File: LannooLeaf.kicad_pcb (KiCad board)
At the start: 2 copper layers, 348.4 x 351.9 mm, 167 parts, among them J1 Conn_01x01, J12 Conn_02x04_Counter_Clockwise, J2 Conn_01x01, J3 Conn_01x01, J4 Conn_01x01, J5 Conn_02x04_Counter_Clockwise, J6 Conn_02x10_Counter_Clockwise, J7 Conn_02x10_Counter_Clockwise

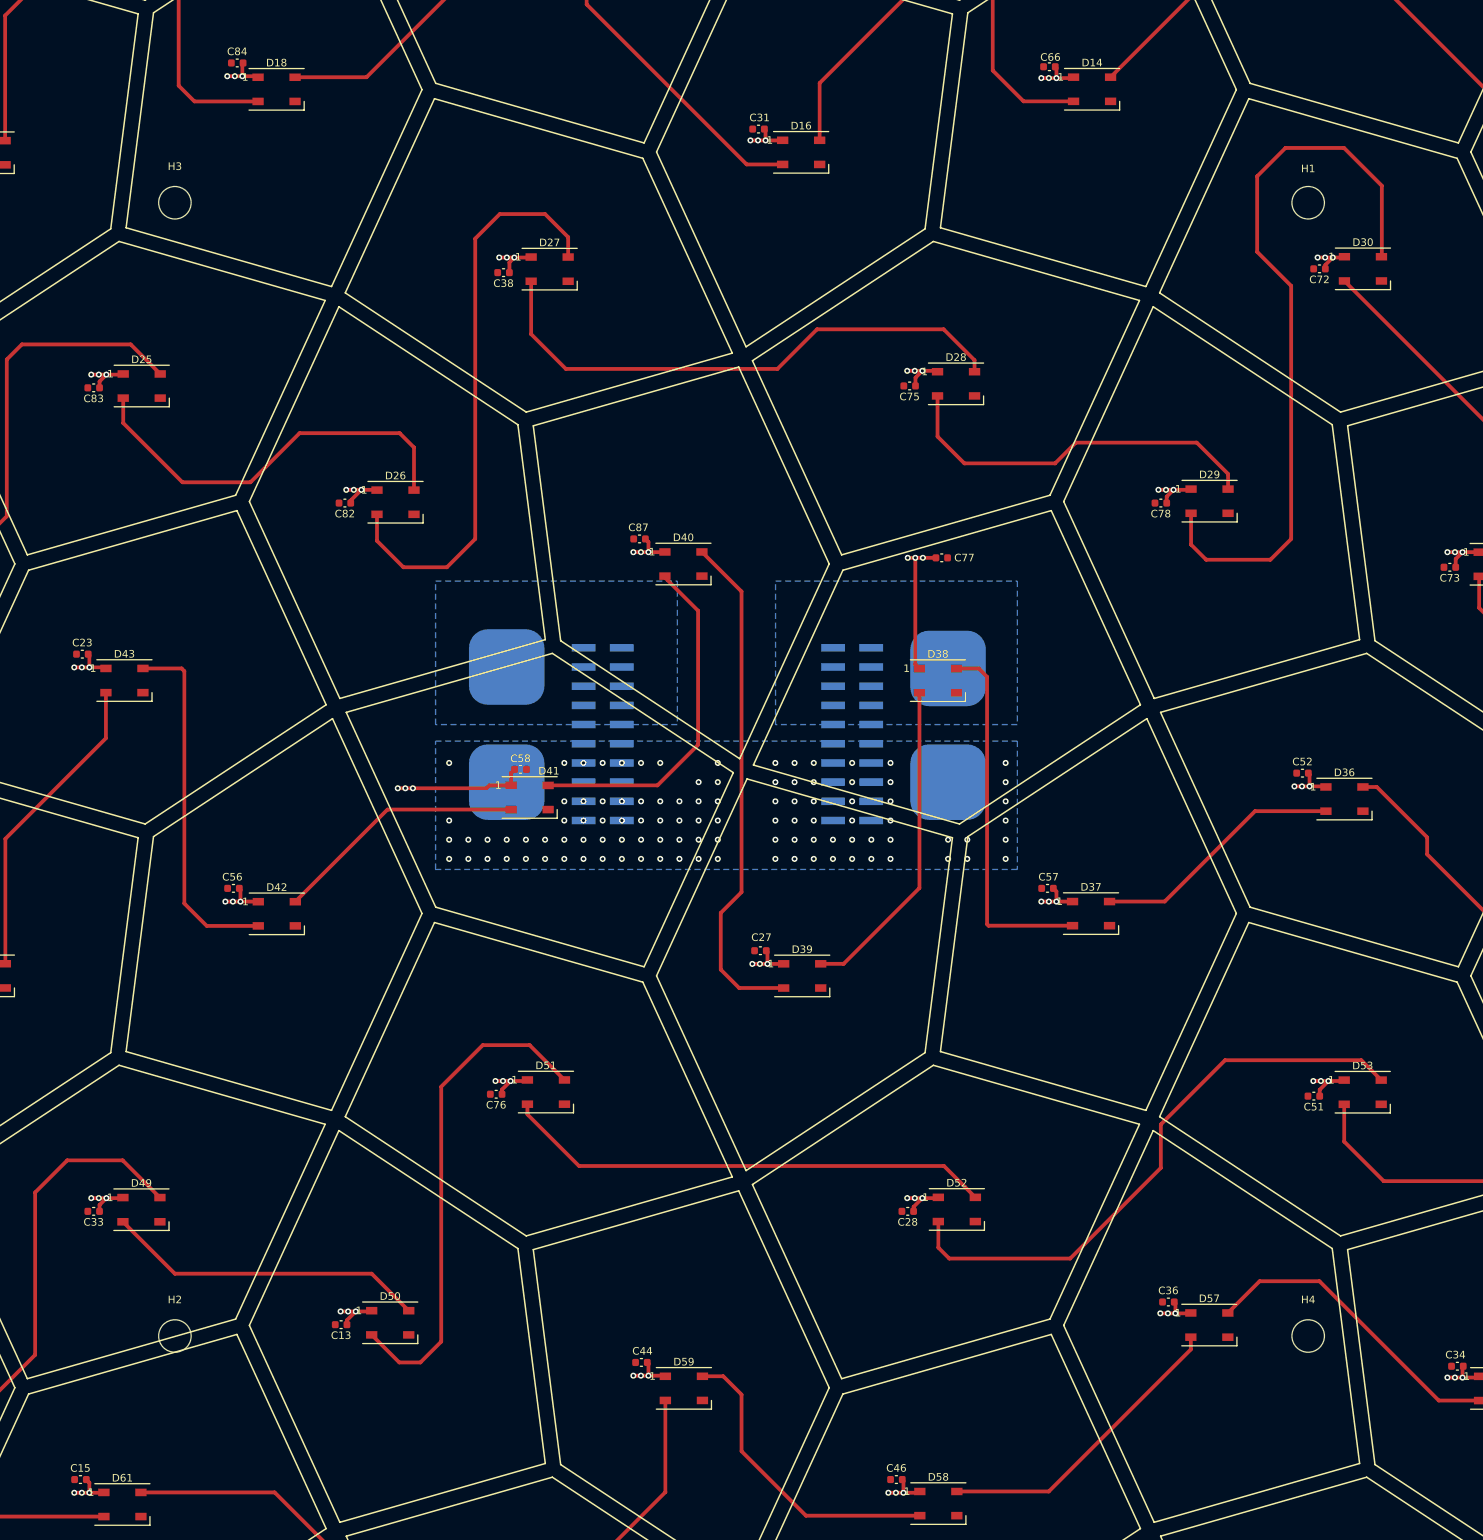
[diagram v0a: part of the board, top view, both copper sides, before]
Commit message: update mountingholes
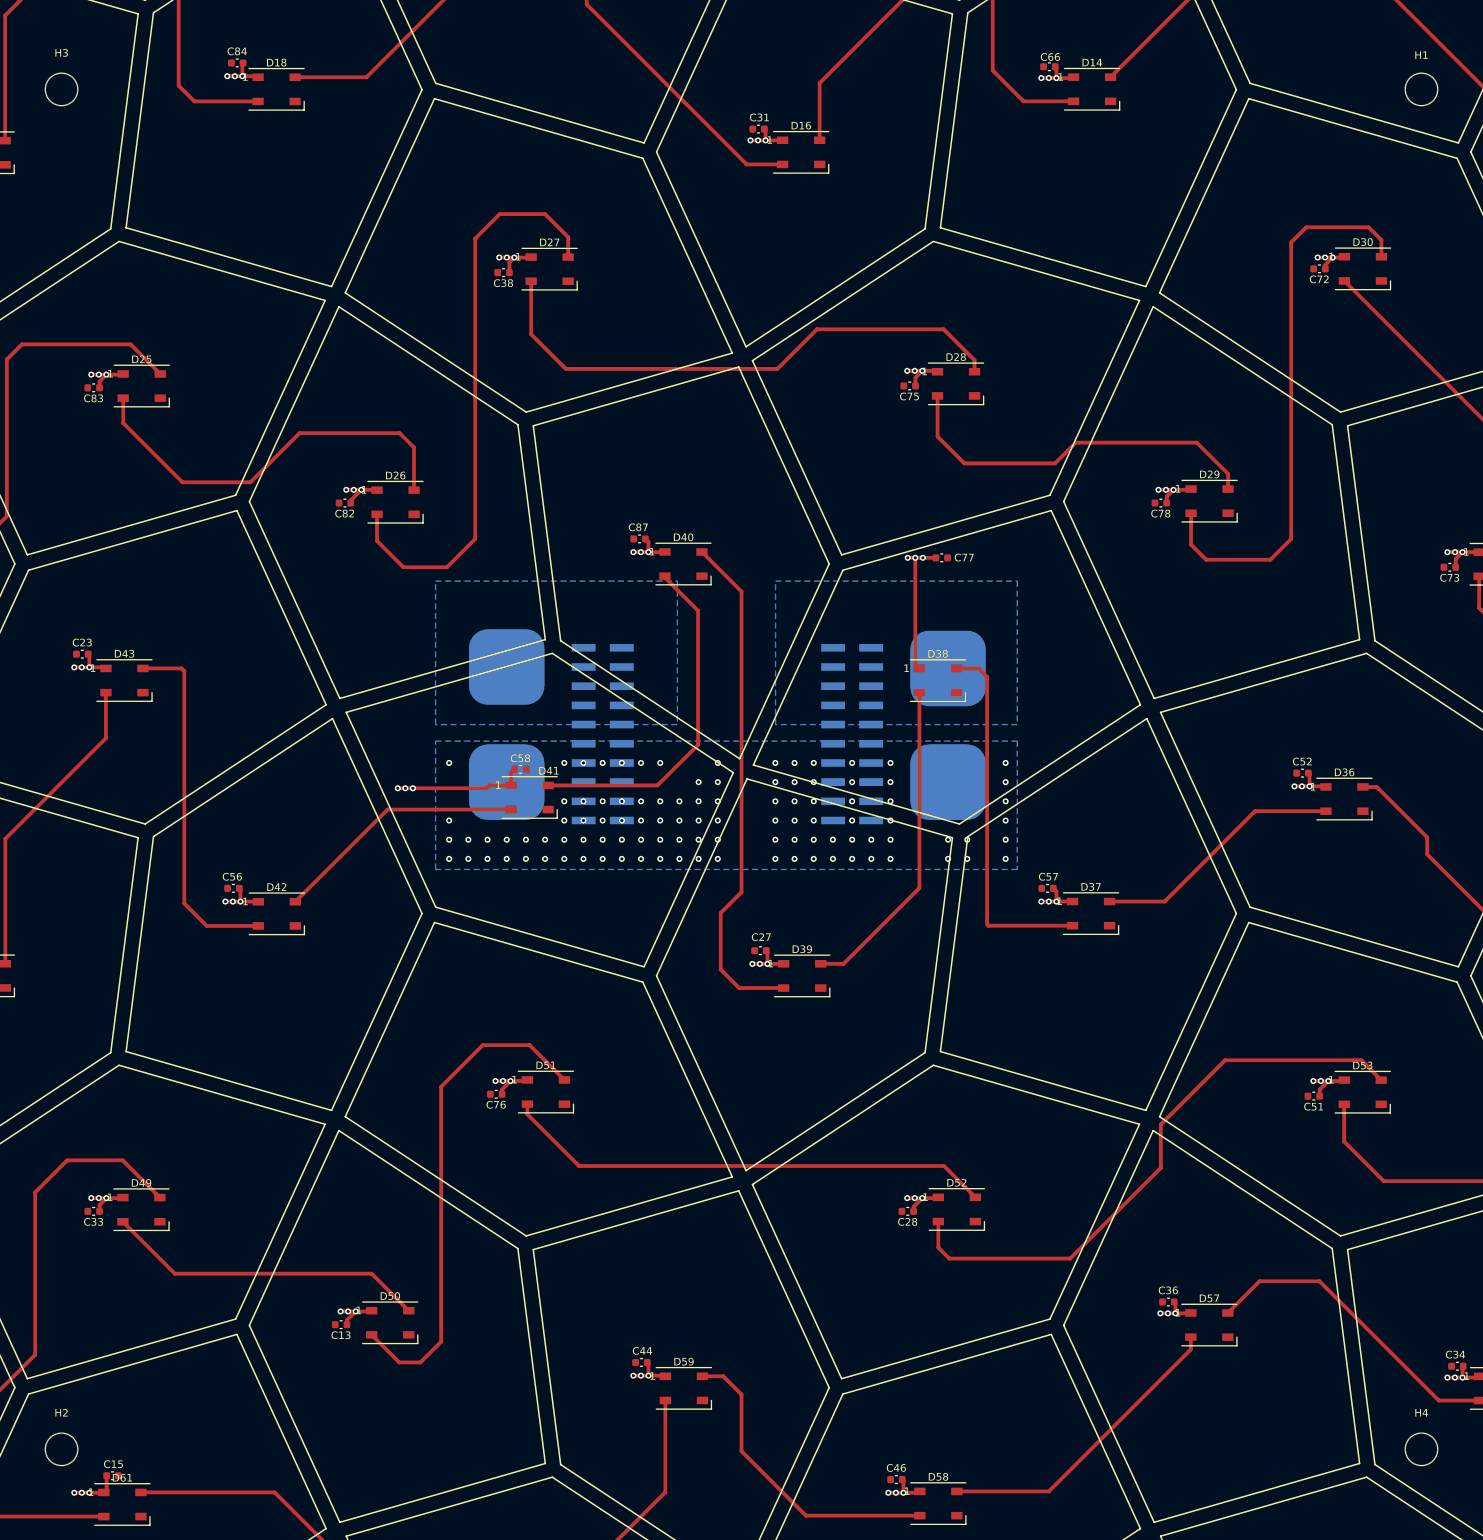
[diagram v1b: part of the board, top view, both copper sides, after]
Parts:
- moved H7 33.3 mm to (164.3, 95.1)
- moved H5 33.2 mm to (214.2, 94.2)
- moved H6 33.2 mm to (266.0, 94.5)
- moved H1 21.2 mm to (306.5, 126.8)
- moved H2 21.2 mm to (126.5, 306.8)
- moved H3 21.2 mm to (126.5, 126.8)
- moved H4 21.2 mm to (306.5, 306.8)
- moved C15 4.28 mm to (133.2, 310.2), turned to 0 degrees
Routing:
- net Net-(D29-Pad2): track 98.8 -> 74.3 mm
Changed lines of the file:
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@@
   )
   (footprint "MountingHole:MountingHole_4.3mm_M4_ISO14580" (layer "F.Cu")
-    (at 291.5 141.75)
+    (at 306.5 126.75)
     (descr "Mounting Hole 4.3mm, no annular, M4, ISO14580")
     (tags "mounting hole 4.3mm no annular m4 iso14580")
@@
   )
   (footprint "MountingHole:MountingHole_4.3mm_M4_ISO7380" (layer "F.Cu")
-    (at 141.5 141.75)
+    (at 126.5 126.75)
     (descr "Mounting Hole 4.3mm, no annular, M4, ISO7380")
     (tags "mounting hole 4.3mm no annular m4 iso7380")
@@
   )
   (footprint "Capacitor_SMD:C_0603_1608Metric" (layer "F.Cu")
-    (at 129 310.75 180)
+    (at 133.25 310.25)
     (descr "Capacitor SMD 0603 (1608 Metric), square (rectangular) end terminal, IPC_7351 nominal, (Body size source: IPC-SM-782 page 76, https://www.pcb-3d.com/wordpress/wp-content/uploads/ipc-sm-782a_amendment_1_and_2.pdf), generated with kicad-footprint-generator")
     (tags "capacitor")
@@
     (property "Sheetname" "Primitive Unit1")
     (attr smd)
-    (fp_text reference "C15" (at 0 1.5) (layer "F.SilkS")
+    (fp_text reference "C15" (at 0.14058 -1.5) (layer "F.SilkS")
       (effects (font (size 1 1) (thickness 0.15)))
     )
@@
     (fp_line (start -0.8 0.4) (end -0.8 -0.4) (layer "F.Fab") (width 0.1))
     (fp_line (start 0.8 0.4) (end -0.8 0.4) (layer "F.Fab") (width 0.1))
-    (pad "1" smd roundrect locked (at -0.775 0 180) (size 0.9 0.95) (layers "F.Cu" "F.Paste" "F.Mask") (roundrect_rratio 0.25)
+    (pad "1" smd roundrect locked (at -0.775 0) (size 0.9 0.95) (layers "F.Cu" "F.Paste" "F.Mask") (roundrect_rratio 0.25)
       (net 4 "+5V") (pintype "passive"))
-    (pad "2" smd roundrect locked (at 0.775 0 180) (size 0.9 0.95) (layers "F.Cu" "F.Paste" "F.Mask") (roundrect_rratio 0.25)
+    (pad "2" smd roundrect locked (at 0.775 0) (size 0.9 0.95) (layers "F.Cu" "F.Paste" "F.Mask") (roundrect_rratio 0.25)
       (net 1 "GND") (pintype "passive"))
     (model "${KICAD6_3DMODEL_DIR}/Capacitor_SMD.3dshapes/C_0603_1608Metric.wrl"
@@
   )
   (footprint "MountingHole:MountingHole_4.3mm_M4_ISO7380" (layer "F.Cu")
-    (at 291.5 291.75)
+    (at 306.5 306.75)
     (descr "Mounting Hole 4.3mm, no annular, M4, ISO7380")
     (tags "mounting hole 4.3mm no annular m4 iso7380")
@@
   )
   (footprint "MountingHole:MountingHole_4.3mm_M4_ISO7380" (layer "F.Cu")
-    (at 141.5 291.75)
+    (at 126.5 306.75)
     (descr "Mounting Hole 4.3mm, no annular, M4, ISO7380")
     (tags "mounting hole 4.3mm no annular m4 iso7380")
@@
   )
   (footprint "LannooLeaf:Logo" (layer "B.Cu")
-    (at 214.25 127.5 180)
+    (at 214.25 94.25 180)
     (property "Sheetfile" "LannooLeaf.kicad_sch")
     (property "Sheetname" "")
@@
   )
   (footprint "LannooLeaf:logo_devbit_15mm" (layer "B.Cu")
-    (at 164.340863 128.370133 180)
+    (at 164.340863 95.120133 180)
     (property "Sheetfile" "LannooLeaf.kicad_sch")
     (property "Sheetname" "")
@@
   )
   (footprint "LannooLeaf:logo-vives" (layer "B.Cu")
-    (at 266 127.75 180)
+    (at 266 94.5 180)
     (property "Sheetfile" "LannooLeaf.kicad_sch")
     (property "Sheetname" "")
@@
   (gr_line locked (start 149.542334 180.467014) (end 161.389328 154.682549) (layer "User.1") (width 0.2))
   (gr_line locked (start 162.234052 261.885609) (end 174.208607 235.822823) (layer "User.1") (width 0.2))
-  (gr_rect (start 291.5 291.75) (end 141.5 141.75) (layer "User.8") (width 0.15) (fill none))
-  (gr_text "Jonas Lannoo\nSille Van Landschoot" (at 240.75 140) (layer "B.SilkS")
+  (gr_rect (start 306.5 306.75) (end 126.5 126.75) (layer "User.8") (width 0.15) (fill none))
+  (gr_text "Jonas Lannoo\nSille Van Landschoot" (at 240.75 106.75) (layer "B.SilkS")
     (effects (font (size 1 1) (thickness 0.15)) (justify left mirror))
   )
-  (gr_text "LannooLeaf Panel V1.0" (at 223.5 136.75) (layer "B.SilkS")
+  (gr_text "LannooLeaf Panel V1.0" (at 223.5 103.5) (layer "B.SilkS")
     (effects (font (size 2 2) (thickness 0.15)) (justify mirror))
   )
   (dimension (type aligned) (layer "User.2")
+    (pts (xy 126.5 306.75) (xy 306.5 306.75))
+    (height 10)
+    (gr_text "180 mm" (at 216.5 313.6) (layer "User.2")
+      (effects (font (size 3 3) (thickness 0.15)))
+    )
+    (format (units 3) (units_format 1) (precision 0))
+    (style (thickness 0.15) (arrow_length 3) (text_position_mode 0) (extension_height 0.58642) (extension_offset 0.5) keep_text_aligned)
+  )
+  (dimension (type aligned) (layer "User.2")
+    (pts (xy 306.5 306.75) (xy 306.5 126.75))
+    (height 4.88542)
+    (gr_text "180 mm" (at 316.5 216.75 90) (layer "User.2")
+      (effects (font (size 3 3) (thickness 0.15)))
+    )
+    (format (units 3) (units_format 1) (precision 0))
+    (style (thickness 0.15) (arrow_length 3) (text_position_mode 2) (extension_height 0.58642) (extension_offset 0.5) keep_text_aligned)
+  )
+  (dimension (type aligned) (layer "User.2")
     (pts (xy 195.58 223.84) (xy 228.6 223.84))
     (height 7.3)
@@
   (segment (start 202.18 79) (end 206.5 79) (width 0.5) (layer "F.Cu") (net 4))
   (segment (start 184.43 149) (end 188.75 149) (width 0.5) (layer "F.Cu") (net 4))
-  (segment (start 130.18 311.155) (end 129.775 310.75) (width 0.5) (layer "F.Cu") (net 4))
   (segment (start 347.525 165.75) (end 347.525 164.725) (width 0.5) (layer "F.Cu") (net 4))
   (segment (start 327.43 242.5) (end 327.43 241.155) (width 0.5) (layer "F.Cu") (net 4))
@@
   (segment (start 150.18 234.25) (end 150.18 232.655) (width 0.5) (layer "F.Cu") (net 4))
   (segment (start 219.68 132.155) (end 219.525 132) (width 0.5) (layer "F.Cu") (net 4))
+  (segment (start 132.475 312.075) (end 132.1 312.45) (width 0.5) (layer "F.Cu") (net 4))
   (segment (start 219.68 133.5) (end 219.68 132.155) (width 0.5) (layer "F.Cu") (net 4))
   (segment (start 96.25 78.25) (end 96.25 77.525) (width 0.5) (layer "F.Cu") (net 4))
@@
   (segment (start 293.025 259.155) (end 294.18 258) (width 0.5) (layer "F.Cu") (net 4))
   (segment (start 166.025 69.25) (end 166.025 70.655) (width 0.5) (layer "F.Cu") (net 4))
-  (segment (start 130.18 312.5) (end 130.18 311.155) (width 0.5) (layer "F.Cu") (net 4))
   (segment (start 309.93 79) (end 314.25 79) (width 0.5) (layer "F.Cu") (net 4))
   (segment (start 239.525 164.905) (end 240.43 164) (width 0.5) (layer "F.Cu") (net 4))
@@
   (segment (start 347.68 55.25) (end 347.68 53.845) (width 0.5) (layer "F.Cu") (net 4))
   (segment (start 289.68 219) (end 294 219) (width 0.5) (layer "F.Cu") (net 4))
+  (segment (start 132.475 310.25) (end 132.475 312.075) (width 0.5) (layer "F.Cu") (net 4))
   (segment (start 363.93 125.25) (end 368.25 125.25) (width 0.5) (layer "F.Cu") (net 4))
   (segment (start 58.18 287.155) (end 58.025 287) (width 0.5) (layer "F.Cu") (net 4))
@@
   (segment (start 242.44 172.69) (end 246 176.25) (width 0.5) (layer "F.Cu") (net 31))
   (segment (start 276.75 173.5) (end 280.9 177.65) (width 0.5) (layer "F.Cu") (net 31))
-  (segment (start 276 187) (end 278 189) (width 0.5) (layer "F.Cu") (net 32))
-  (segment (start 296.25 134.5) (end 301.25 139.5) (width 0.5) (layer "F.Cu") (net 32))
-  (segment (start 289.25 152.75) (end 284.75 148.25) (width 0.5) (layer "F.Cu") (net 32))
-  (segment (start 289.25 186.25) (end 289.25 152.75) (width 0.5) (layer "F.Cu") (net 32))
-  (segment (start 284.75 148.25) (end 284.75 138.25) (width 0.5) (layer "F.Cu") (net 32))
-  (segment (start 301.25 148.85) (end 301.2 148.9) (width 0.5) (layer "F.Cu") (net 32))
-  (segment (start 288.5 134.5) (end 296.25 134.5) (width 0.5) (layer "F.Cu") (net 32))
-  (segment (start 284.75 138.25) (end 288.5 134.5) (width 0.5) (layer "F.Cu") (net 32))
+  (segment (start 289.25 186.25) (end 289.25 147) (width 0.5) (layer "F.Cu") (net 32))
+  (segment (start 289.25 147) (end 291.25 145) (width 0.5) (layer "F.Cu") (net 32))
   (segment (start 278 189) (end 286.5 189) (width 0.5) (layer "F.Cu") (net 32))
   (segment (start 276 182.85) (end 276 187) (width 0.5) (layer "F.Cu") (net 32))
+  (segment (start 299.5 145) (end 301.2 146.7) (width 0.5) (layer "F.Cu") (net 32))
   (segment (start 286.5 189) (end 289.25 186.25) (width 0.5) (layer "F.Cu") (net 32))
-  (segment (start 301.25 139.5) (end 301.25 148.85) (width 0.5) (layer "F.Cu") (net 32))
+  (segment (start 291.25 145) (end 299.5 145) (width 0.5) (layer "F.Cu") (net 32))
+  (segment (start 276 187) (end 278 189) (width 0.5) (layer "F.Cu") (net 32))
+  (segment (start 301.2 146.7) (end 301.2 148.9) (width 0.5) (layer "F.Cu") (net 32))
   (segment (start 296.3 152.1) (end 319.03 174.83) (width 0.5) (layer "F.Cu") (net 33))
   (segment (start 319.03 174.83) (end 319.03 188) (width 0.5) (layer "F.Cu") (net 33))

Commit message: update labels
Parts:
- removed kibuzzard-62A832D2: G***, kibuzzard-62A832D2
- removed kibuzzard-62A832E7: G***, kibuzzard-62A832E7
- removed kibuzzard-62A832FB: G***, kibuzzard-62A832FB
- removed kibuzzard-62A8330D: G***, kibuzzard-62A8330D
- added kibuzzard-62A843C0: G***, kibuzzard-62A843C0, B.Cu at (222.5, 214.5)
- added kibuzzard-62A843EA: G***, kibuzzard-62A843EA, B.Cu at (206.8, 214.5)
- added kibuzzard-62A8440B: G***, kibuzzard-62A8440B, B.Cu at (206.8, 200.8)
- added kibuzzard-62A84432: G***, kibuzzard-62A84432, B.Cu at (222.2, 200.8)

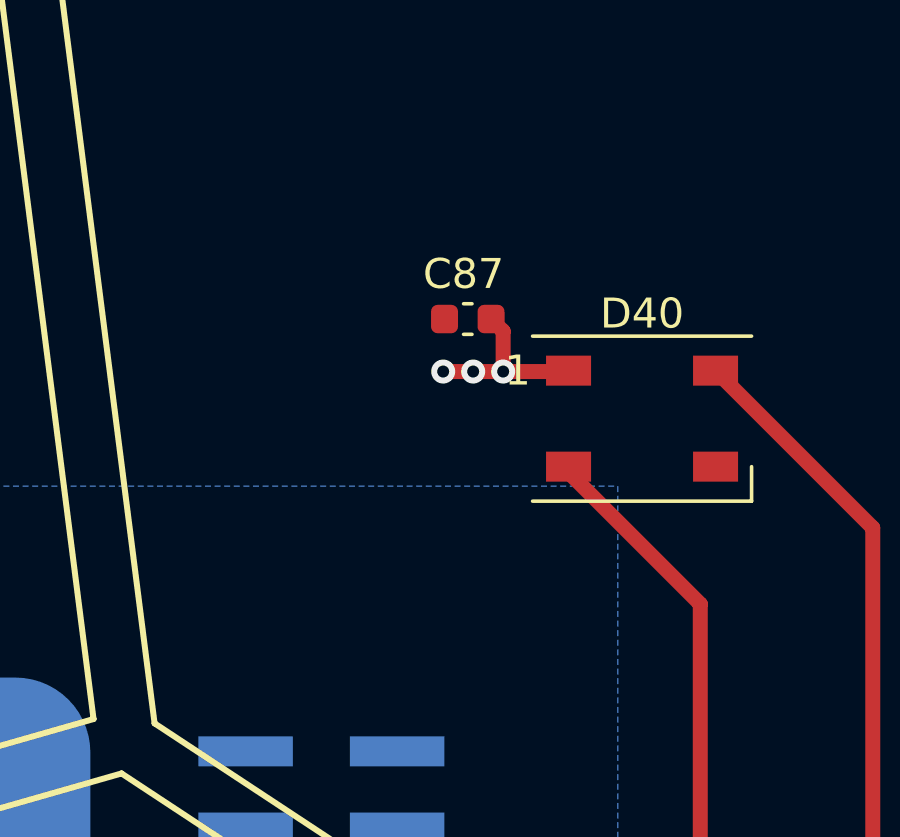
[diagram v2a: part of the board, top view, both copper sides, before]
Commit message: add extra 5V caps
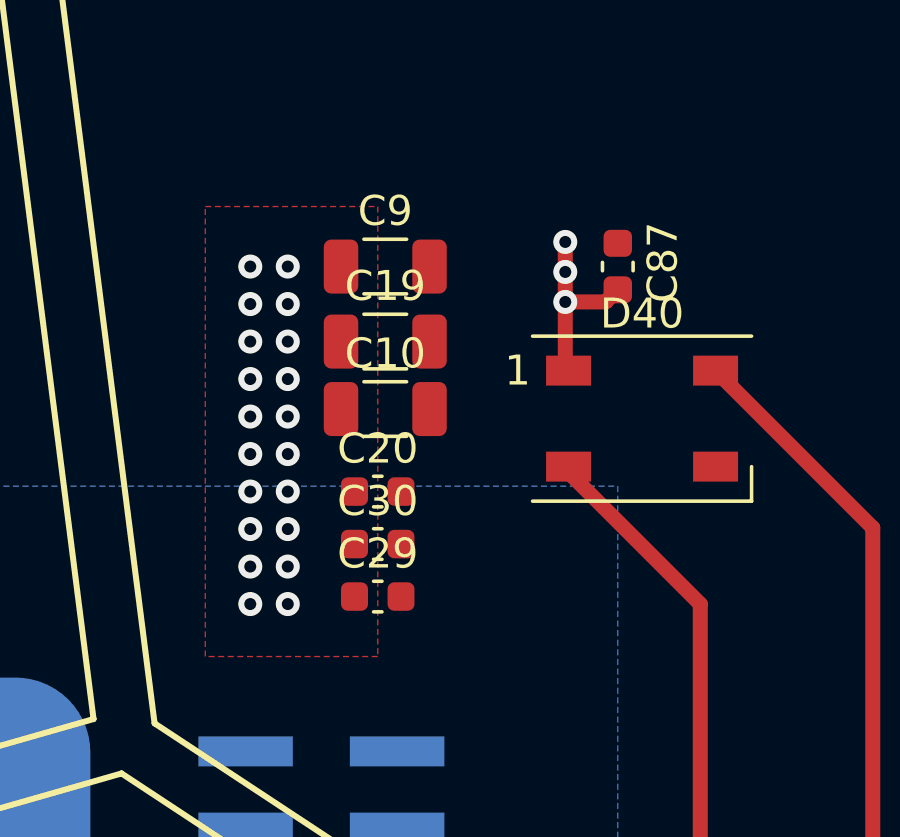
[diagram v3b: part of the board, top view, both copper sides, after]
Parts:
- added C10: 22uF, Capacitor_SMD:C_1206_3216Metric, F.Cu at (200.2, 189.2)
- added C19: 22uF, Capacitor_SMD:C_1206_3216Metric, F.Cu at (200.2, 187.0)
- added C20: 1uF, Capacitor_SMD:C_0603_1608Metric, F.Cu at (200.0, 192.0)
- added C29: 1uF, Capacitor_SMD:C_0603_1608Metric, F.Cu at (200.0, 195.5)
- added C30: 1uF, Capacitor_SMD:C_0603_1608Metric, F.Cu at (200.0, 193.8)
- added C9: 22uF, Capacitor_SMD:C_1206_3216Metric, F.Cu at (200.2, 184.5)
- moved C87 5.30 mm to (208.0, 184.5), turned to 90 degrees
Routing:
- net +5V: vias 216 -> 236
- added copper zone on F.Cu, net +5V
